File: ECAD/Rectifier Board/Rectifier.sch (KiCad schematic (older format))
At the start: 18 parts

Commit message: Update Rectifier.sch
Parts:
- removed C?: 1000uF, symbol Device:CP
- J?: value 120VAC -> MAINS
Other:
- moved on the sheet: C?, D?, J?, L?, R?, T?, U?

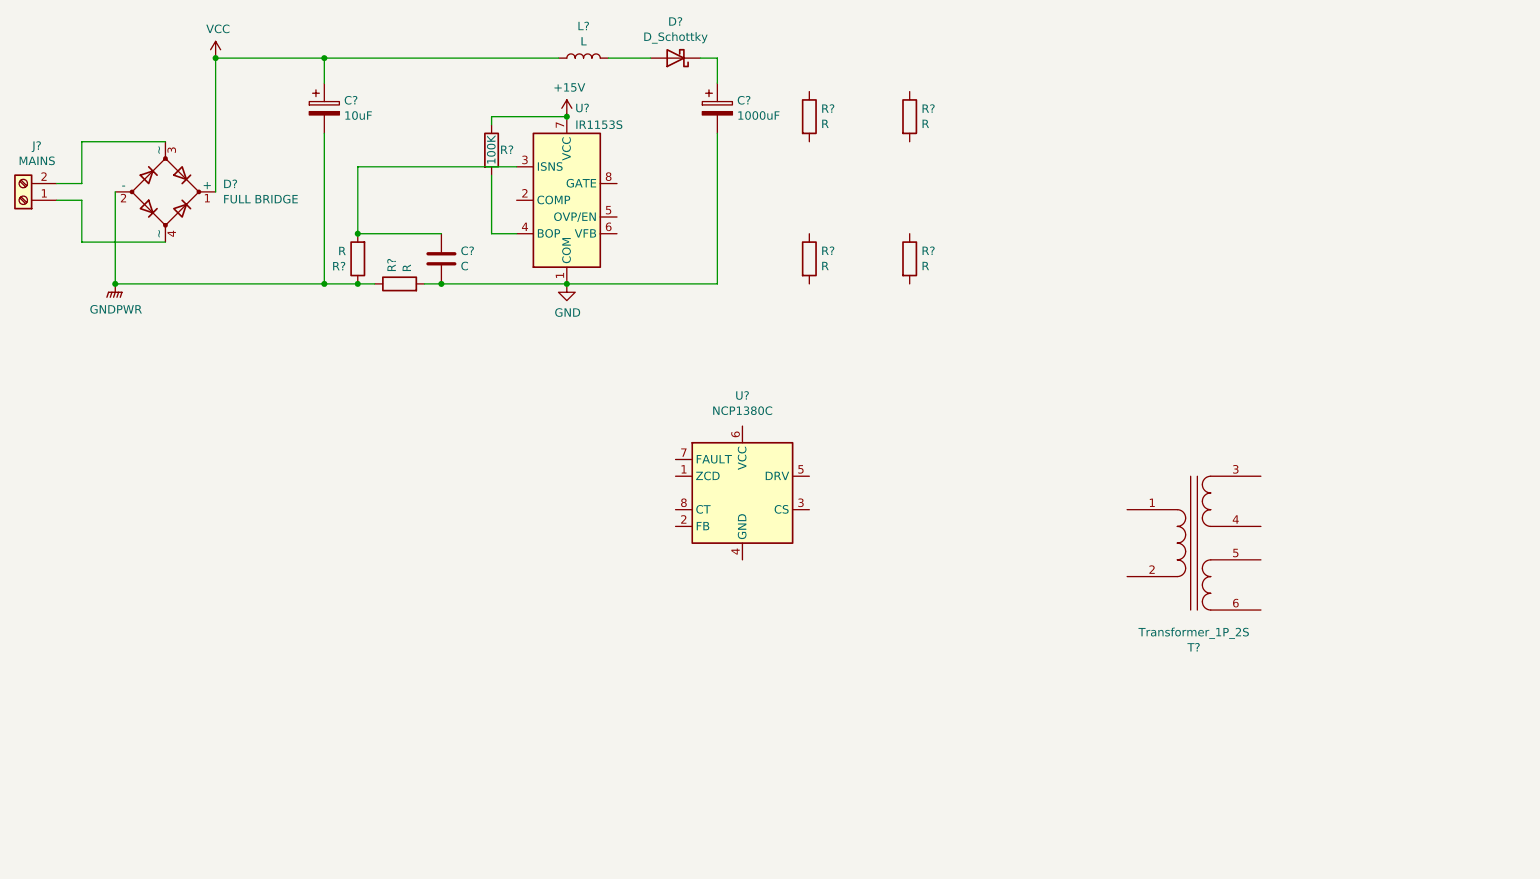
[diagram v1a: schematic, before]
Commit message: Second pass on power board, some minor edit to rectifier sch
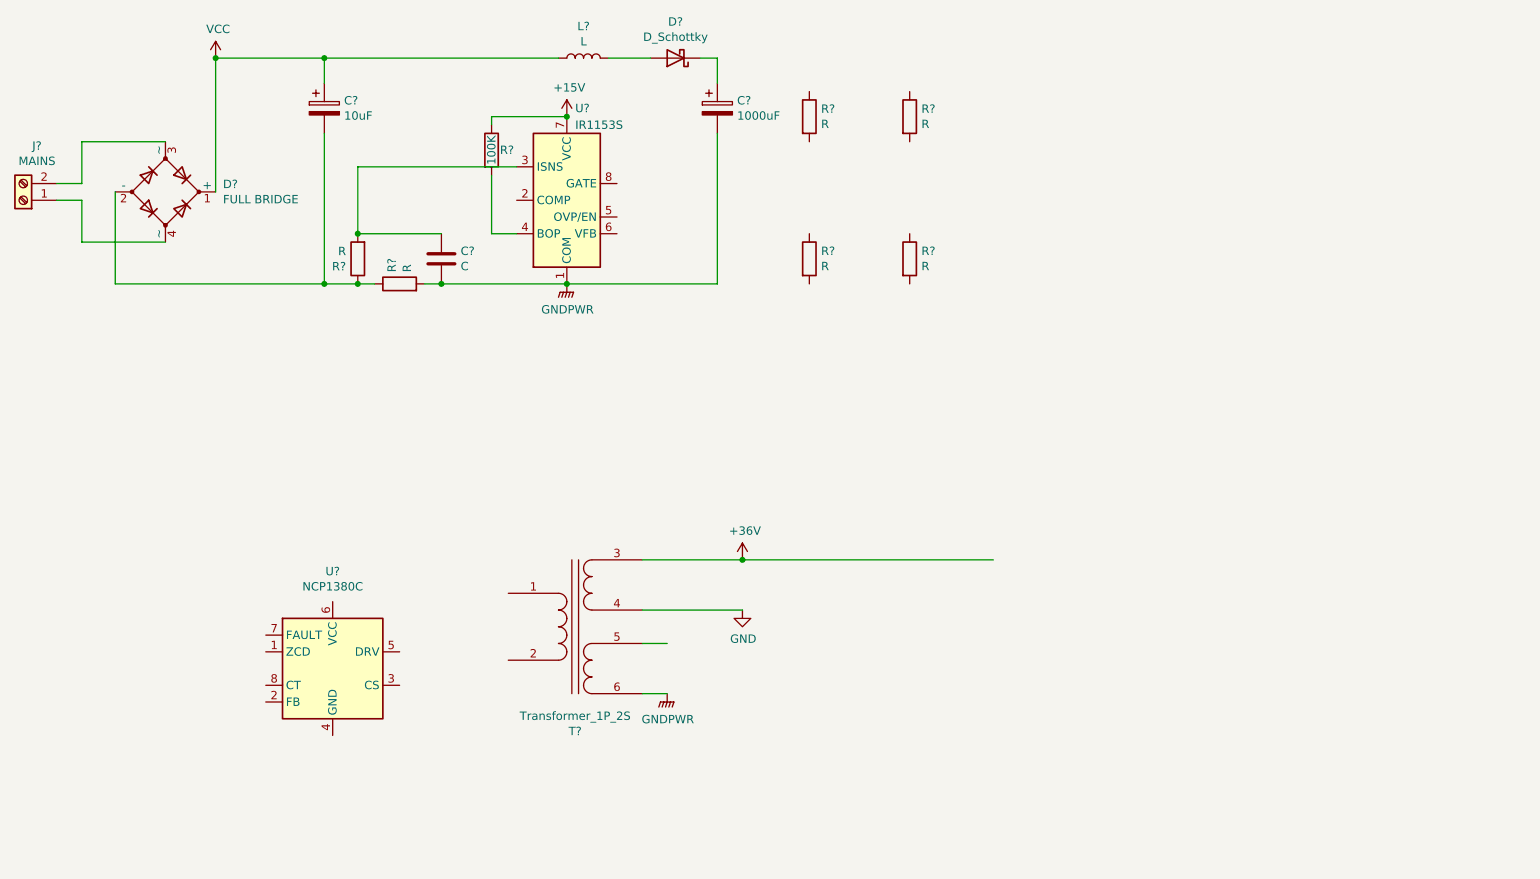
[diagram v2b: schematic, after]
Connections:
- net labels added: +36V
- wire segments 29 -> 34
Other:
- moved on the sheet: T?, U?
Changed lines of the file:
@@
 L power:GND #PWR?
 U 1 1 6205A908
-P 4000 2250
-F 0 "#PWR?" H 4000 2000 50  0001 C CNN
-F 1 "GND" H 4005 2077 50  0000 C CNN
-F 2 "" H 4000 2250 50  0001 C CNN
-F 3 "" H 4000 2250 50  0001 C CNN
-	1    4000 2250
+P 5050 4200
+F 0 "#PWR?" H 5050 3950 50  0001 C CNN
+F 1 "GND" H 5055 4027 50  0000 C CNN
+F 2 "" H 5050 4200 50  0001 C CNN
+F 3 "" H 5050 4200 50  0001 C CNN
+	1    5050 4200
 	1    0    0    -1
 $EndComp
@@
 L power:GNDPWR #PWR?
 U 1 1 62119A04
-P 1300 2250
-F 0 "#PWR?" H 1300 2050 50  0001 C CNN
-F 1 "GNDPWR" H 1304 2096 50  0000 C CNN
-F 2 "" H 1300 2200 50  0001 C CNN
-F 3 "" H 1300 2200 50  0001 C CNN
-	1    1300 2250
+P 4000 2250
+F 0 "#PWR?" H 4000 2050 50  0001 C CNN
+F 1 "GNDPWR" H 4004 2096 50  0000 C CNN
+F 2 "" H 4000 2200 50  0001 C CNN
+F 3 "" H 4000 2200 50  0001 C CNN
+	1    4000 2250
 	1    0    0    -1
 $EndComp
 Wire Wire Line
 	1300 2250 2550 2250
-Connection ~ 1300 2250
 Wire Wire Line
 	3250 2250 4000 2250
@@
 L Regulator_Controller:NCP1380C U?
 U 1 1 6212BD3D
-P 5050 3500
-F 0 "U?" H 5050 4081 50  0000 C CNN
-F 1 "NCP1380C" H 5050 3990 50  0000 C CNN
-F 2 "Package_SO:SOIC-8_3.9x4.9mm_P1.27mm" H 5050 3500 50  0001 C CIN
-F 3 "https://www.onsemi.com/pub/Collateral/NCP1380-D.PDF" H 5050 3500 50  0001 C CNN
-	1    5050 3500
+P 2600 4550
+F 0 "U?" H 2600 5131 50  0000 C CNN
+F 1 "NCP1380C" H 2600 5040 50  0000 C CNN
+F 2 "Package_SO:SOIC-8_3.9x4.9mm_P1.27mm" H 2600 4550 50  0001 C CIN
+F 3 "https://www.onsemi.com/pub/Collateral/NCP1380-D.PDF" H 2600 4550 50  0001 C CNN
+	1    2600 4550
 	1    0    0    -1
 $EndComp
@@
 L Device:Transformer_1P_2S T?
 U 1 1 6213DB4F
-P 7750 3800
-F 0 "T?" H 7750 3175 50  0000 C CNN
-F 1 "Transformer_1P_2S" H 7750 3266 50  0000 C CNN
-F 2 "" H 7750 3800 50  0001 C CNN
-F 3 "~" H 7750 3800 50  0001 C CNN
-	1    7750 3800
+P 4050 4300
+F 0 "T?" H 4050 3675 50  0000 C CNN
+F 1 "Transformer_1P_2S" H 4050 3766 50  0000 C CNN
+F 2 "" H 4050 4300 50  0001 C CNN
+F 3 "~" H 4050 4300 50  0001 C CNN
+	1    4050 4300
 	1    0    0    -1
 $EndComp
@@
 	-1   0    0    1
 $EndComp
+Wire Wire Line
+	5050 4200 4450 4200
+$Comp
+L power:GNDPWR #PWR?
+U 1 1 621C5C53
+P 4600 4700
+F 0 "#PWR?" H 4600 4500 50  0001 C CNN
+F 1 "GNDPWR" H 4604 4546 50  0000 C CNN
+F 2 "" H 4600 4650 50  0001 C CNN
+F 3 "" H 4600 4650 50  0001 C CNN
+	1    4600 4700
+	1    0    0    -1
+$EndComp
+Wire Wire Line
+	4600 4700 4450 4700
+Wire Wire Line
+	4450 4400 4600 4400
+Wire Wire Line
+	4450 3900 5050 3900
+$Comp
+L power:+36V #PWR?
+U 1 1 621C9846
+P 5050 3900
+F 0 "#PWR?" H 5050 3750 50  0001 C CNN
+F 1 "+36V" H 5065 4073 50  0000 C CNN
+F 2 "" H 5050 3900 50  0001 C CNN
+F 3 "" H 5050 3900 50  0001 C CNN
+	1    5050 3900
+	1    0    0    -1
+$EndComp
+Connection ~ 5050 3900
+Wire Wire Line
+	5050 3900 6550 3900
 $EndSCHEMATC

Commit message: place components for apfc
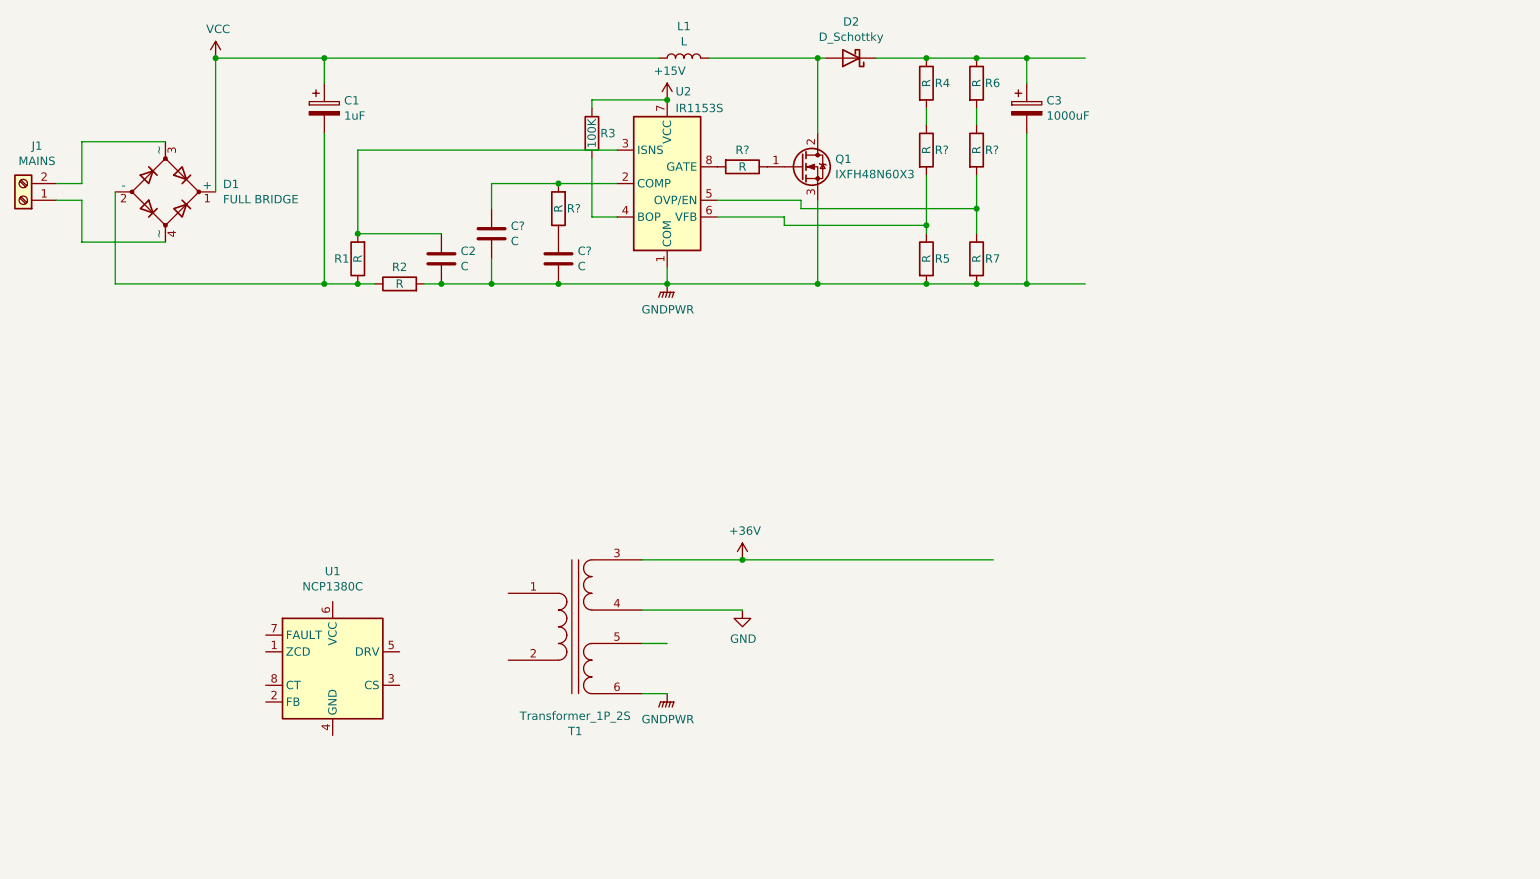
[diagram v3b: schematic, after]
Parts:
- added C? (x2): C, symbol Device:C
- added Q1: IXFH48N60X3, Package_TO_SOT_THT:TO-247-3_Vertical, symbol Transistor_FET:C3M0065090D
- added R? (x4): R, symbol Device:R
- C1: renamed from C?; value 10uF -> 1uF
- gave numbers to parts that had none: 16
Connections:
- wire segments 34 -> 63
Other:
- moved on the sheet: C3, D2, L1, R3, R4, R5, R6, R7, U2

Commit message: Component selection
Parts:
- added C6, C7: 470uF, symbol Device:CP
- added U?: TL494, symbol Regulator_Controller:TL494
- C1: value 1uF -> .47uF
- C2: value C -> 1nF
- C3: renamed from C?; value C -> 6.8nF
- C4: renamed from C?; value C -> 2.8uF
- C5: renamed from C3; value 1000uF -> 470uF
- L1: value L -> 1mH
- R1: value R -> 100R
- R10, R7: renamed from R?; value R -> 1M
- R11: renamed from R7; value R -> 36.5K
- R2: value R -> 90m
- R3: renamed from R?; value R -> 6.65K
- R5: renamed from R?; value R -> 100R
- R6: renamed from R4; value R -> 1M
- R8: renamed from R5; value R -> 37.4K
- R9: renamed from R6; value R -> 1M
- renumbered R3 to R4
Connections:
- wire segments 63 -> 69
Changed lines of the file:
@@
 	1300 1700 1300 2250
 $Comp
-L power:GND #PWR0101
+L power:GND #PWR06
 U 1 1 6205A908
 P 5050 4200
-F 0 "#PWR0101" H 5050 3950 50  0001 C CNN
+F 0 "#PWR06" H 5050 3950 50  0001 C CNN
 F 1 "GND" H 5055 4027 50  0000 C CNN
 F 2 "" H 5050 4200 50  0001 C CNN
@@
 $EndComp
 $Comp
-L power:VCC #PWR0102
+L power:VCC #PWR01
 U 1 1 6205AED4
 P 1900 900
-F 0 "#PWR0102" H 1900 750 50  0001 C CNN
+F 0 "#PWR01" H 1900 750 50  0001 C CNN
 F 1 "VCC" H 1915 1073 50  0000 C CNN
 F 2 "" H 1900 900 50  0001 C CNN
@@
 P 4700 900
 F 0 "L1" V 4890 900 50  0000 C CNN
-F 1 "L" V 4799 900 50  0000 C CNN
+F 1 "1mH" V 4799 900 50  0000 C CNN
 F 2 "" H 4700 900 50  0001 C CNN
 F 3 "~" H 4700 900 50  0001 C CNN
@@
 $EndComp
 $Comp
-L Device:R R4
+L Device:R R6
 U 1 1 62108E47
 P 6150 1050
-F 0 "R4" H 6200 1050 50  0000 L CNN
-F 1 "R" V 6150 1050 50  0000 C CNN
+F 0 "R6" H 6200 1050 50  0000 L CNN
+F 1 "1M" V 6150 1050 50  0000 C CNN
 F 2 "" V 6080 1050 50  0001 C CNN
 F 3 "~" H 6150 1050 50  0001 C CNN
@@
 $EndComp
 $Comp
-L Device:R R5
+L Device:R R8
 U 1 1 621099B6
 P 6150 2100
-F 0 "R5" H 6200 2100 50  0000 L CNN
-F 1 "R" V 6150 2100 50  0000 C CNN
+F 0 "R8" H 6200 2100 50  0000 L CNN
+F 1 "37.4K" V 6150 2100 50  0000 C CNN
 F 2 "" V 6080 2100 50  0001 C CNN
 F 3 "~" H 6150 2100 50  0001 C CNN
@@
 $EndComp
 $Comp
-L Device:CP C3
+L Device:CP C5
 U 1 1 62109F4A
 P 6750 1200
-F 0 "C3" H 6868 1246 50  0000 L CNN
-F 1 "1000uF" H 6868 1155 50  0000 L CNN
+F 0 "C5" H 6868 1246 50  0000 L CNN
+F 1 "470uF" H 6868 1155 50  0000 L CNN
 F 2 "" H 6788 1050 50  0001 C CNN
 F 3 "~" H 6750 1200 50  0001 C CNN
@@
 $EndComp
 $Comp
-L Device:R R6
+L Device:R R9
 U 1 1 6210AF02
 P 6450 1050
-F 0 "R6" H 6500 1050 50  0000 L CNN
-F 1 "R" V 6450 1050 50  0000 C CNN
+F 0 "R9" H 6500 1050 50  0000 L CNN
+F 1 "1M" V 6450 1050 50  0000 C CNN
 F 2 "" V 6380 1050 50  0001 C CNN
 F 3 "~" H 6450 1050 50  0001 C CNN
@@
 $EndComp
 $Comp
-L Device:R R7
+L Device:R R11
 U 1 1 6210AF08
 P 6450 2100
-F 0 "R7" H 6500 2100 50  0000 L CNN
-F 1 "R" V 6450 2100 50  0000 C CNN
+F 0 "R11" H 6500 2100 50  0000 L CNN
+F 1 "36.5K" V 6450 2100 50  0000 C CNN
 F 2 "" V 6380 2100 50  0001 C CNN
 F 3 "~" H 6450 2100 50  0001 C CNN
@@
 P 3000 2250
 F 0 "R2" V 3100 2250 50  0000 C CNN
-F 1 "R" V 3000 2250 50  0000 C CNN
+F 1 "90m" V 3000 2250 50  0000 C CNN
 F 2 "" V 2930 2250 50  0001 C CNN
 F 3 "~" H 3000 2250 50  0001 C CNN
@@
 P 2750 2100
 F 0 "R1" H 2800 2100 50  0000 L CNN
-F 1 "R" V 2750 2100 50  0000 C CNN
+F 1 "100R" V 2750 2100 50  0000 C CNN
 F 2 "" V 2680 2100 50  0001 C CNN
 F 3 "~" H 2750 2100 50  0001 C CNN
@@
 P 3250 2100
 F 0 "C2" H 3365 2146 50  0000 L CNN
-F 1 "C" H 3365 2055 50  0000 L CNN
+F 1 "1nF" H 3365 2055 50  0000 L CNN
 F 2 "" H 3288 1950 50  0001 C CNN
 F 3 "~" H 3250 2100 50  0001 C CNN
@@
 	1900 900  1900 1700
 $Comp
-L power:GNDPWR #PWR0104
+L power:GNDPWR #PWR03
 U 1 1 62119A04
 P 4600 2250
-F 0 "#PWR0104" H 4600 2050 50  0001 C CNN
+F 0 "#PWR03" H 4600 2050 50  0001 C CNN
 F 1 "GNDPWR" H 4604 2096 50  0000 C CNN
 F 2 "" H 4600 2200 50  0001 C CNN
@@
 P 2550 1200
 F 0 "C1" H 2668 1246 50  0000 L CNN
-F 1 "1uF" H 2668 1155 50  0000 L CNN
+F 1 ".47uF" H 2668 1155 50  0000 L CNN
 F 2 "" H 2588 1050 50  0001 C CNN
 F 3 "~" H 2550 1200 50  0001 C CNN
@@
 	5050 4200 4450 4200
 $Comp
-L power:GNDPWR #PWR0105
+L power:GNDPWR #PWR04
 U 1 1 621C5C53
 P 4600 4700
-F 0 "#PWR0105" H 4600 4500 50  0001 C CNN
+F 0 "#PWR04" H 4600 4500 50  0001 C CNN
 F 1 "GNDPWR" H 4604 4546 50  0000 C CNN
 F 2 "" H 4600 4650 50  0001 C CNN
@@
 	4450 3900 5050 3900
 $Comp
-L power:+36V #PWR0106
+L power:+36V #PWR05
 U 1 1 621C9846
 P 5050 3900
-F 0 "#PWR0106" H 5050 3750 50  0001 C CNN
+F 0 "#PWR05" H 5050 3750 50  0001 C CNN
 F 1 "+36V" H 5065 4073 50  0000 C CNN
 F 2 "" H 5050 3900 50  0001 C CNN
@@
 $EndComp
 $Comp
-L Device:R R?
+L Device:R R5
 U 1 1 621CF40A
 P 5050 1550
-F 0 "R?" V 4950 1550 50  0000 C CNN
-F 1 "R" V 5050 1550 50  0000 C CNN
+F 0 "R5" V 4950 1550 50  0000 C CNN
+F 1 "100R" V 5050 1550 50  0000 C CNN
 F 2 "" V 4980 1550 50  0001 C CNN
 F 3 "~" H 5050 1550 50  0001 C CNN
@@
 $EndComp
 $Comp
-L Device:C C?
+L Device:C C4
 U 1 1 621D2771
 P 3950 2100
-F 0 "C?" H 4065 2146 50  0000 L CNN
-F 1 "C" H 4065 2055 50  0000 L CNN
+F 0 "C4" H 4065 2146 50  0000 L CNN
+F 1 "2.8uF" H 4065 2055 50  0000 L CNN
 F 2 "" H 3988 1950 50  0001 C CNN
 F 3 "~" H 3950 2100 50  0001 C CNN
@@
 	4600 2250 5500 2250
 $Comp
-L Device:R R?
+L Device:R R7
 U 1 1 621DCAE0
 P 6150 1450
-F 0 "R?" H 6200 1450 50  0000 L CNN
-F 1 "R" V 6150 1450 50  0000 C CNN
+F 0 "R7" H 6200 1450 50  0000 L CNN
+F 1 "1M" V 6150 1450 50  0000 C CNN
 F 2 "" V 6080 1450 50  0001 C CNN
 F 3 "~" H 6150 1450 50  0001 C CNN
@@
 $EndComp
 $Comp
-L Device:R R?
+L Device:R R10
 U 1 1 621DCAE6
 P 6450 1450
-F 0 "R?" H 6500 1450 50  0000 L CNN
-F 1 "R" V 6450 1450 50  0000 C CNN
+F 0 "R10" H 6500 1450 50  0000 L CNN
+F 1 "1M" V 6450 1450 50  0000 C CNN
 F 2 "" V 6380 1450 50  0001 C CNN
 F 3 "~" H 6450 1450 50  0001 C CNN
@@
 	6150 900  6450 900
 Connection ~ 6750 900
-Wire Wire Line
-	6750 900  7100 900
-Connection ~ 6750 2250
-Wire Wire Line
-	6750 2250 7100 2250
-$Comp
-L Device:C C?
+$Comp
+L Device:C C3
 U 1 1 621FEDE5
 P 3550 1950
-F 0 "C?" H 3665 1996 50  0000 L CNN
-F 1 "C" H 3665 1905 50  0000 L CNN
+F 0 "C3" H 3665 1996 50  0000 L CNN
+F 1 "6.8nF" H 3665 1905 50  0000 L CNN
 F 2 "" H 3588 1800 50  0001 C CNN
 F 3 "~" H 3550 1950 50  0001 C CNN
@@
 $EndComp
 $Comp
-L Device:R R?
+L Device:R R3
 U 1 1 621FFE1F
 P 3950 1800
-F 0 "R?" H 3900 1800 50  0000 R CNN
-F 1 "R" V 3950 1800 50  0000 C CNN
+F 0 "R3" H 3900 1800 50  0000 R CNN
+F 1 "6.65K" V 3950 1800 50  0000 C CNN
 F 2 "" V 3880 1800 50  0001 C CNN
 F 3 "~" H 3950 1800 50  0001 C CNN
@@
 	4600 1150 4150 1150
 $Comp
-L Device:R R3
+L Device:R R4
 U 1 1 6211CBE0
 P 4150 1350
-F 0 "R3" H 4200 1350 50  0000 L CNN
+F 0 "R4" H 4200 1350 50  0000 L CNN
 F 1 "100K" V 4150 1350 50  0000 C CNN
 F 2 "" V 4080 1350 50  0001 C CNN
@@
 $EndComp
 $Comp
-L power:+15V #PWR0103
+L power:+15V #PWR02
 U 1 1 6206D895
 P 4600 1150
-F 0 "#PWR0103" H 4600 1000 50  0001 C CNN
+F 0 "#PWR02" H 4600 1000 50  0001 C CNN
 F 1 "+15V" H 4615 1323 50  0000 C CNN
 F 2 "" H 4600 1150 50  0001 C CNN
@@
 Wire Wire Line
 	3550 2250 3950 2250
+$Comp
+L Device:CP C6
+U 1 1 621D8082
+P 7250 1200
+F 0 "C6" H 7368 1246 50  0000 L CNN
+F 1 "470uF" H 7368 1155 50  0000 L CNN
+F 2 "" H 7288 1050 50  0001 C CNN
+F 3 "~" H 7250 1200 50  0001 C CNN
+	1    7250 1200
+	1    0    0    -1
+$EndComp
+Wire Wire Line
+	7250 1050 7250 900
+Wire Wire Line
+	7250 1350 7250 2250
+$Comp
+L Device:CP C7
+U 1 1 621D9935
+P 7750 1200
+F 0 "C7" H 7868 1246 50  0000 L CNN
+F 1 "470uF" H 7868 1155 50  0000 L CNN
+F 2 "" H 7788 1050 50  0001 C CNN
+F 3 "~" H 7750 1200 50  0001 C CNN
+	1    7750 1200
+	1    0    0    -1
+$EndComp
+Wire Wire Line
+	7750 1050 7750 900
+Wire Wire Line
+	7750 1350 7750 2250
+Wire Wire Line
+	6750 900  7250 900
+Connection ~ 7250 900
+Wire Wire Line
+	7250 900  7750 900
+Wire Wire Line
+	7750 2250 7250 2250
+Connection ~ 6750 2250
+Connection ~ 7250 2250
+Wire Wire Line
+	7250 2250 6750 2250
+$Comp
+L Regulator_Controller:TL494 U?
+U 1 1 621DF2F3
+P 7950 4700
+F 0 "U?" H 7950 5581 50  0000 C CNN
+F 1 "TL494" H 7950 5490 50  0000 C CNN
+F 2 "" H 7950 4700 50  0001 C CNN
+F 3 "http://www.ti.com/lit/ds/symlink/tl494.pdf" H 7950 4700 50  0001 C CNN
+	1    7950 4700
+	1    0    0    -1
+$EndComp
 $EndSCHEMATC
